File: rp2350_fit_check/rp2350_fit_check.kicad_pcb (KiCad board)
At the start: 6 copper layers, 118.8 x 73.4 mm, 364 parts, among them J1 Conn_01x05, J2 Conn_01x05, J3 Conn_01x05, J4 Conn_01x05, J5 Conn_01x04, SW1 SW_Push, SW2 SW_Push, U1 AP2112K-3.3, U2 RP2040, U3 W25Q16JVUXIQ_TR, Y1 12MHz

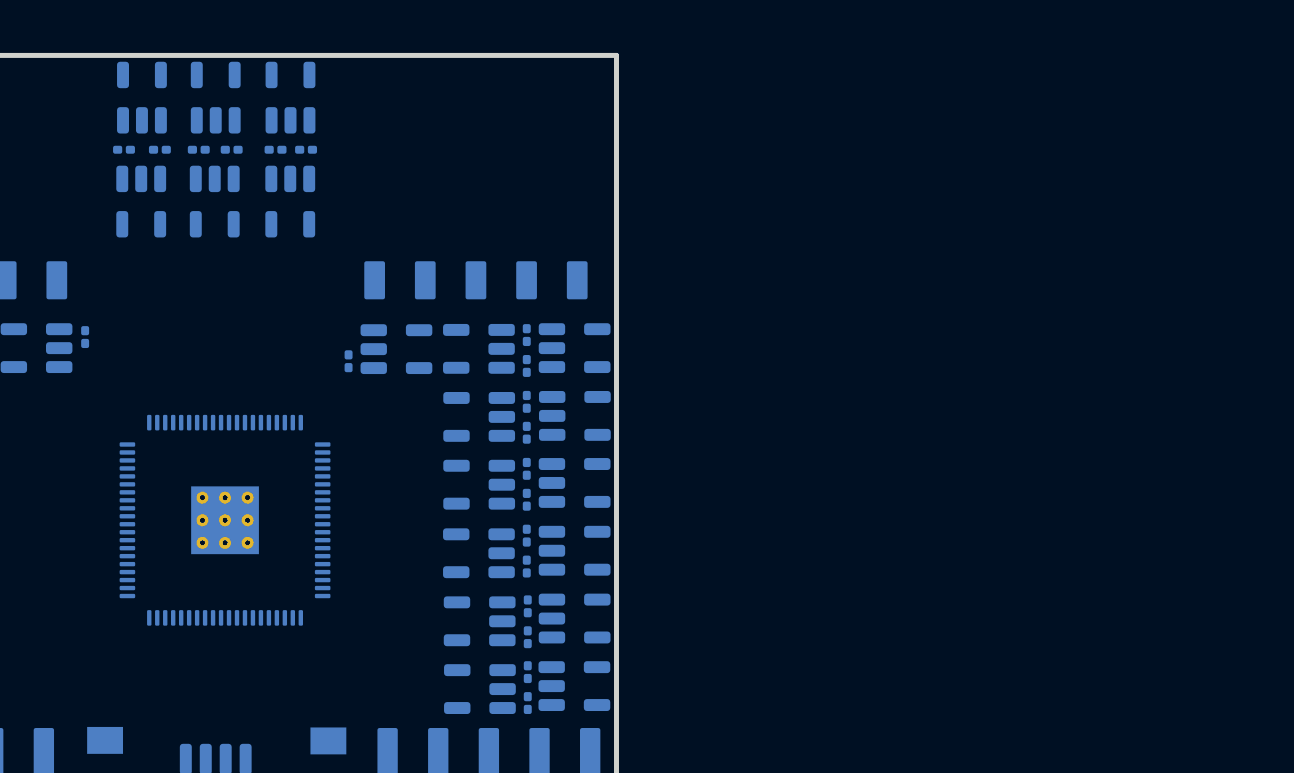
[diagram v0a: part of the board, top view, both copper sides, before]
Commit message: More work on rp2350 fit check.
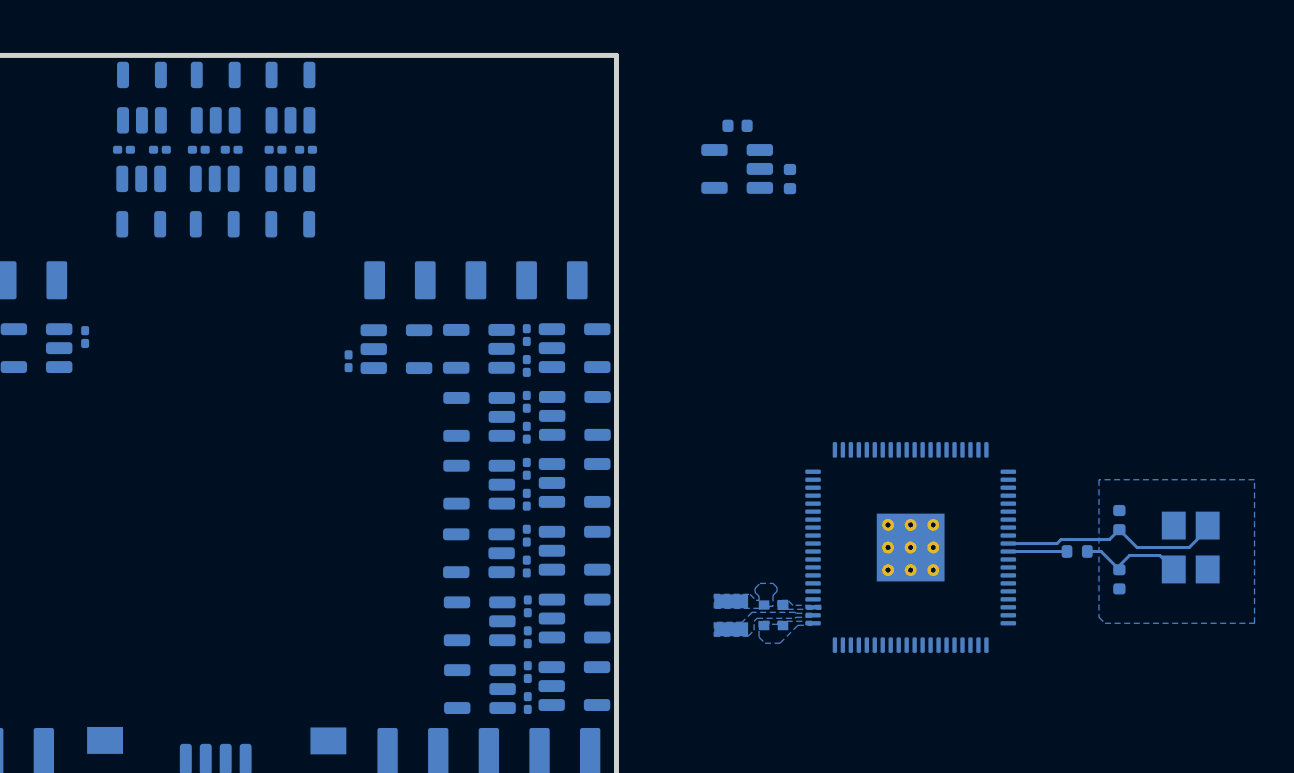
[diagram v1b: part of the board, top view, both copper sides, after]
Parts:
- added ?: , , B.Cu at (177.1, 110.6)
- added C1: 10uF, panel_custom:C_0402_1005Metric, B.Cu at (177.4, 89.3)
- added C2: 10uF, panel_custom:C_0402_1005Metric, B.Cu at (174.8, 86.6)
- added C3: 15p, Capacitor_SMD:C_0402_1005Metric, B.Cu at (194.0, 106.4)
- added C4: 15p, Capacitor_SMD:C_0402_1005Metric, B.Cu at (194.0, 109.3)
- added C6: 4.7u, RP2350_80QFN_minimal:C_0402_1005Metric_small_pads, B.Cu at (177.1, 111.2)
- added C7: 4.7u, RP2350_80QFN_minimal:C_0402_1005Metric_small_pads, B.Cu at (176.2, 111.2)
- added L1: 3.3u, RP2350_80QFN_minimal:L_pol_2016, B.Cu at (174.5, 111.2)
- added R2: 1k, Resistor_SMD:R_0402_1005Metric, B.Cu at (191.9, 108.0)
- added U1: AP2112K-3.3, Package_TO_SOT_SMD:SOT-23-5, B.Cu at (174.8, 88.8)
- added Y1: ABM8-272-T3, Crystal:Crystal_SMD_3225-4Pin_3.2x2.5mm, B.Cu at (197.6, 107.8)
- moved REF** 34.4 mm to (183.5, 107.8), turned to -90 degrees
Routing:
- net /XIN: track 0.00 -> 11.1 mm
- net Net-(C4-Pad1): track 0.00 -> 5.25 mm
- net /XOUT: track 0.00 -> 2.93 mm
- added copper zone on B.Cu, net +1V1
- added copper zone on B.Cu, net +3V3
- added copper zone on B.Cu, net /VREG_LX
- added copper zone on B.Cu, net GND

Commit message: Worked more on fit check / preliminary layout.
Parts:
- removed the C3 at (194.0, 106.4)
- removed the C4 at (194.0, 109.3)
- removed the R2 at (191.9, 108.0)
- added D1: LED, panel_custom:LED_0402_1005Metric, F.Cu at (130.0, 84.5)
- added D10: LED, panel_custom:LED_0402_1005Metric, F.Cu at (130.0, 107.0)
- added D100: LED, panel_custom:LED_0402_1005Metric, F.Cu at (145.0, 92.0)
- added D101: LED, panel_custom:LED_0402_1005Metric, F.Cu at (145.0, 94.5)
- added D102: LED, panel_custom:LED_0402_1005Metric, F.Cu at (145.0, 97.0)
- added D103: LED, panel_custom:LED_0402_1005Metric, F.Cu at (145.0, 99.5)
- added D104: LED, panel_custom:LED_0402_1005Metric, F.Cu at (145.0, 102.0)
- added D105: LED, panel_custom:LED_0402_1005Metric, F.Cu at (145.0, 104.5)
- added D106: LED, panel_custom:LED_0402_1005Metric, F.Cu at (145.0, 107.0)
- added D107: LED, panel_custom:LED_0402_1005Metric, F.Cu at (145.0, 109.5)
- added D108: LED, panel_custom:LED_0402_1005Metric, F.Cu at (145.0, 112.0)
- added D109: LED, panel_custom:LED_0402_1005Metric, F.Cu at (145.0, 114.5)
- added D11: LED, panel_custom:LED_0402_1005Metric, F.Cu at (130.0, 109.5)
- added D110: LED, panel_custom:LED_0402_1005Metric, F.Cu at (145.0, 117.0)
- added D111: LED, panel_custom:LED_0402_1005Metric, F.Cu at (145.0, 119.5)
- added D112: LED, panel_custom:LED_0402_1005Metric, F.Cu at (145.0, 122.0)
- added D113: LED, panel_custom:LED_0402_1005Metric, F.Cu at (147.5, 84.5)
- added D114: LED, panel_custom:LED_0402_1005Metric, F.Cu at (147.5, 87.0)
- added D115: LED, panel_custom:LED_0402_1005Metric, F.Cu at (147.5, 89.5)
- added D116: LED, panel_custom:LED_0402_1005Metric, F.Cu at (147.5, 92.0)
- added D117: LED, panel_custom:LED_0402_1005Metric, F.Cu at (147.5, 94.5)
- added D118: LED, panel_custom:LED_0402_1005Metric, F.Cu at (147.5, 97.0)
- added D119: LED, panel_custom:LED_0402_1005Metric, F.Cu at (147.5, 99.5)
- added D12: LED, panel_custom:LED_0402_1005Metric, F.Cu at (130.0, 112.0)
- added D120: LED, panel_custom:LED_0402_1005Metric, F.Cu at (147.5, 102.0)
- added D121: LED, panel_custom:LED_0402_1005Metric, F.Cu at (147.5, 104.5)
- added D122: LED, panel_custom:LED_0402_1005Metric, F.Cu at (147.5, 107.0)
- added D123: LED, panel_custom:LED_0402_1005Metric, F.Cu at (147.5, 109.5)
- added D124: LED, panel_custom:LED_0402_1005Metric, F.Cu at (147.5, 112.0)
- added D125: LED, panel_custom:LED_0402_1005Metric, F.Cu at (147.5, 114.5)
- added D126: LED, panel_custom:LED_0402_1005Metric, F.Cu at (147.5, 117.0)
- added D127: LED, panel_custom:LED_0402_1005Metric, F.Cu at (147.5, 119.5)
- added D128: LED, panel_custom:LED_0402_1005Metric, F.Cu at (147.5, 122.0)
- added D129: LED, panel_custom:LED_0402_1005Metric, F.Cu at (150.0, 84.5)
- added D13: LED, panel_custom:LED_0402_1005Metric, F.Cu at (130.0, 114.5)
- added D130: LED, panel_custom:LED_0402_1005Metric, F.Cu at (150.0, 87.0)
- added D131: LED, panel_custom:LED_0402_1005Metric, F.Cu at (150.0, 89.5)
- added D132: LED, panel_custom:LED_0402_1005Metric, F.Cu at (150.0, 92.0)
- added D133: LED, panel_custom:LED_0402_1005Metric, F.Cu at (150.0, 94.5)
- added D134: LED, panel_custom:LED_0402_1005Metric, F.Cu at (150.0, 97.0)
- added D135: LED, panel_custom:LED_0402_1005Metric, F.Cu at (150.0, 99.5)
- added D136: LED, panel_custom:LED_0402_1005Metric, F.Cu at (150.0, 102.0)
- added D137: LED, panel_custom:LED_0402_1005Metric, F.Cu at (150.0, 104.5)
- added D138: LED, panel_custom:LED_0402_1005Metric, F.Cu at (150.0, 107.0)
- added D139: LED, panel_custom:LED_0402_1005Metric, F.Cu at (150.0, 109.5)
- added D14: LED, panel_custom:LED_0402_1005Metric, F.Cu at (130.0, 117.0)
- added D140: LED, panel_custom:LED_0402_1005Metric, F.Cu at (150.0, 112.0)
- added D141: LED, panel_custom:LED_0402_1005Metric, F.Cu at (150.0, 114.5)
- added D142: LED, panel_custom:LED_0402_1005Metric, F.Cu at (150.0, 117.0)
- added D143: LED, panel_custom:LED_0402_1005Metric, F.Cu at (150.0, 119.5)
- added D144: LED, panel_custom:LED_0402_1005Metric, F.Cu at (150.0, 122.0)
- added D145: LED, panel_custom:LED_0402_1005Metric, F.Cu at (152.5, 84.5)
- added D146: LED, panel_custom:LED_0402_1005Metric, F.Cu at (152.5, 87.0)
- added D147: LED, panel_custom:LED_0402_1005Metric, F.Cu at (152.5, 89.5)
- added D148: LED, panel_custom:LED_0402_1005Metric, F.Cu at (152.5, 92.0)
- added D149: LED, panel_custom:LED_0402_1005Metric, F.Cu at (152.5, 94.5)
- added D15: LED, panel_custom:LED_0402_1005Metric, F.Cu at (130.0, 119.5)
- added D150: LED, panel_custom:LED_0402_1005Metric, F.Cu at (152.5, 97.0)
- added D151: LED, panel_custom:LED_0402_1005Metric, F.Cu at (152.5, 99.5)
- added D152: LED, panel_custom:LED_0402_1005Metric, F.Cu at (152.5, 102.0)
- added D153: LED, panel_custom:LED_0402_1005Metric, F.Cu at (152.5, 104.5)
- added D154: LED, panel_custom:LED_0402_1005Metric, F.Cu at (152.5, 107.0)
- added D155: LED, panel_custom:LED_0402_1005Metric, F.Cu at (152.5, 109.5)
- added D156: LED, panel_custom:LED_0402_1005Metric, F.Cu at (152.5, 112.0)
- added D157: LED, panel_custom:LED_0402_1005Metric, F.Cu at (152.5, 114.5)
- added D158: LED, panel_custom:LED_0402_1005Metric, F.Cu at (152.5, 117.0)
- added D159: LED, panel_custom:LED_0402_1005Metric, F.Cu at (152.5, 119.5)
- added D16: LED, panel_custom:LED_0402_1005Metric, F.Cu at (130.0, 122.0)
- added D160: LED, panel_custom:LED_0402_1005Metric, F.Cu at (152.5, 122.0)
- added D161: LED, panel_custom:LED_0402_1005Metric, F.Cu at (155.0, 84.5)
- added D162: LED, panel_custom:LED_0402_1005Metric, F.Cu at (155.0, 87.0)
- added D163: LED, panel_custom:LED_0402_1005Metric, F.Cu at (155.0, 89.5)
- added D164: LED, panel_custom:LED_0402_1005Metric, F.Cu at (155.0, 92.0)
- added D165: LED, panel_custom:LED_0402_1005Metric, F.Cu at (155.0, 94.5)
- added D166: LED, panel_custom:LED_0402_1005Metric, F.Cu at (155.0, 97.0)
- added D167: LED, panel_custom:LED_0402_1005Metric, F.Cu at (155.0, 99.5)
- added D168: LED, panel_custom:LED_0402_1005Metric, F.Cu at (155.0, 102.0)
- added D169: LED, panel_custom:LED_0402_1005Metric, F.Cu at (155.0, 104.5)
- added D17: LED, panel_custom:LED_0402_1005Metric, F.Cu at (132.5, 84.5)
- added D170: LED, panel_custom:LED_0402_1005Metric, F.Cu at (155.0, 107.0)
- added D171: LED, panel_custom:LED_0402_1005Metric, F.Cu at (155.0, 109.5)
- added D172: LED, panel_custom:LED_0402_1005Metric, F.Cu at (155.0, 112.0)
- added D173: LED, panel_custom:LED_0402_1005Metric, F.Cu at (155.0, 114.5)
- added D174: LED, panel_custom:LED_0402_1005Metric, F.Cu at (155.0, 117.0)
- added D175: LED, panel_custom:LED_0402_1005Metric, F.Cu at (155.0, 119.5)
- added D176: LED, panel_custom:LED_0402_1005Metric, F.Cu at (155.0, 122.0)
- added D177: LED, panel_custom:LED_0402_1005Metric, F.Cu at (157.5, 84.5)
- added D178: LED, panel_custom:LED_0402_1005Metric, F.Cu at (157.5, 87.0)
- added D179: LED, panel_custom:LED_0402_1005Metric, F.Cu at (157.5, 89.5)
- added D18: LED, panel_custom:LED_0402_1005Metric, F.Cu at (132.5, 87.0)
- added D180: LED, panel_custom:LED_0402_1005Metric, F.Cu at (157.5, 92.0)
- added D181: LED, panel_custom:LED_0402_1005Metric, F.Cu at (157.5, 94.5)
- added D182: LED, panel_custom:LED_0402_1005Metric, F.Cu at (157.5, 97.0)
- added D183: LED, panel_custom:LED_0402_1005Metric, F.Cu at (157.5, 99.5)
- added D184: LED, panel_custom:LED_0402_1005Metric, F.Cu at (157.5, 102.0)
- added D185: LED, panel_custom:LED_0402_1005Metric, F.Cu at (157.5, 104.5)
- added D186: LED, panel_custom:LED_0402_1005Metric, F.Cu at (157.5, 107.0)
- added D187: LED, panel_custom:LED_0402_1005Metric, F.Cu at (157.5, 109.5)
- added D188: LED, panel_custom:LED_0402_1005Metric, F.Cu at (157.5, 112.0)
- added D189: LED, panel_custom:LED_0402_1005Metric, F.Cu at (157.5, 114.5)
- added D19: LED, panel_custom:LED_0402_1005Metric, F.Cu at (132.5, 89.5)
- added D190: LED, panel_custom:LED_0402_1005Metric, F.Cu at (157.5, 117.0)
- added D191: LED, panel_custom:LED_0402_1005Metric, F.Cu at (157.5, 119.5)
- added D192: LED, panel_custom:LED_0402_1005Metric, F.Cu at (157.5, 122.0)
- added D193: LED, panel_custom:LED_0402_1005Metric, F.Cu at (160.0, 84.5)
- added D194: LED, panel_custom:LED_0402_1005Metric, F.Cu at (160.0, 87.0)
- added D195: LED, panel_custom:LED_0402_1005Metric, F.Cu at (160.0, 89.5)
- added D196: LED, panel_custom:LED_0402_1005Metric, F.Cu at (160.0, 92.0)
- added D197: LED, panel_custom:LED_0402_1005Metric, F.Cu at (160.0, 94.5)
- added D198: LED, panel_custom:LED_0402_1005Metric, F.Cu at (160.0, 97.0)
- added D199: LED, panel_custom:LED_0402_1005Metric, F.Cu at (160.0, 99.5)
- added D2: LED, panel_custom:LED_0402_1005Metric, F.Cu at (130.0, 87.0)
- added D20: LED, panel_custom:LED_0402_1005Metric, F.Cu at (132.5, 92.0)
- added D200: LED, panel_custom:LED_0402_1005Metric, F.Cu at (160.0, 102.0)
- added D201: LED, panel_custom:LED_0402_1005Metric, F.Cu at (160.0, 104.5)
- added D202: LED, panel_custom:LED_0402_1005Metric, F.Cu at (160.0, 107.0)
- added D203: LED, panel_custom:LED_0402_1005Metric, F.Cu at (160.0, 109.5)
- added D204: LED, panel_custom:LED_0402_1005Metric, F.Cu at (160.0, 112.0)
- added D205: LED, panel_custom:LED_0402_1005Metric, F.Cu at (160.0, 114.5)
- added D206: LED, panel_custom:LED_0402_1005Metric, F.Cu at (160.0, 117.0)
- added D207: LED, panel_custom:LED_0402_1005Metric, F.Cu at (160.0, 119.5)
- added D208: LED, panel_custom:LED_0402_1005Metric, F.Cu at (160.0, 122.0)
- added D209: LED, panel_custom:LED_0402_1005Metric, F.Cu at (162.5, 84.5)
- added D21: LED, panel_custom:LED_0402_1005Metric, F.Cu at (132.5, 94.5)
- added D210: LED, panel_custom:LED_0402_1005Metric, F.Cu at (162.5, 87.0)
- added D211: LED, panel_custom:LED_0402_1005Metric, F.Cu at (162.5, 89.5)
- added D212: LED, panel_custom:LED_0402_1005Metric, F.Cu at (162.5, 92.0)
- added D213: LED, panel_custom:LED_0402_1005Metric, F.Cu at (162.5, 94.5)
- added D214: LED, panel_custom:LED_0402_1005Metric, F.Cu at (162.5, 97.0)
- added D215: LED, panel_custom:LED_0402_1005Metric, F.Cu at (162.5, 99.5)
- added D216: LED, panel_custom:LED_0402_1005Metric, F.Cu at (162.5, 102.0)
- added D217: LED, panel_custom:LED_0402_1005Metric, F.Cu at (162.5, 104.5)
- added D218: LED, panel_custom:LED_0402_1005Metric, F.Cu at (162.5, 107.0)
- added D219: LED, panel_custom:LED_0402_1005Metric, F.Cu at (162.5, 109.5)
- added D22: LED, panel_custom:LED_0402_1005Metric, F.Cu at (132.5, 97.0)
- added D220: LED, panel_custom:LED_0402_1005Metric, F.Cu at (162.5, 112.0)
- added D221: LED, panel_custom:LED_0402_1005Metric, F.Cu at (162.5, 114.5)
- added D222: LED, panel_custom:LED_0402_1005Metric, F.Cu at (162.5, 117.0)
- added D223: LED, panel_custom:LED_0402_1005Metric, F.Cu at (162.5, 119.5)
- added D224: LED, panel_custom:LED_0402_1005Metric, F.Cu at (162.5, 122.0)
- added D225: LED, panel_custom:LED_0402_1005Metric, F.Cu at (165.0, 84.5)
- added D226: LED, panel_custom:LED_0402_1005Metric, F.Cu at (165.0, 87.0)
- added D227: LED, panel_custom:LED_0402_1005Metric, F.Cu at (165.0, 89.5)
- added D228: LED, panel_custom:LED_0402_1005Metric, F.Cu at (165.0, 92.0)
- added D229: LED, panel_custom:LED_0402_1005Metric, F.Cu at (165.0, 94.5)
- added D23: LED, panel_custom:LED_0402_1005Metric, F.Cu at (132.5, 99.5)
- added D230: LED, panel_custom:LED_0402_1005Metric, F.Cu at (165.0, 97.0)
- added D231: LED, panel_custom:LED_0402_1005Metric, F.Cu at (165.0, 99.5)
- added D232: LED, panel_custom:LED_0402_1005Metric, F.Cu at (165.0, 102.0)
- added D233: LED, panel_custom:LED_0402_1005Metric, F.Cu at (165.0, 104.5)
- added D234: LED, panel_custom:LED_0402_1005Metric, F.Cu at (165.0, 107.0)
- added D235: LED, panel_custom:LED_0402_1005Metric, F.Cu at (165.0, 109.5)
- added D236: LED, panel_custom:LED_0402_1005Metric, F.Cu at (165.0, 112.0)
- added D237: LED, panel_custom:LED_0402_1005Metric, F.Cu at (165.0, 114.5)
- added D238: LED, panel_custom:LED_0402_1005Metric, F.Cu at (165.0, 117.0)
- added D239: LED, panel_custom:LED_0402_1005Metric, F.Cu at (165.0, 119.5)
- added D24: LED, panel_custom:LED_0402_1005Metric, F.Cu at (132.5, 102.0)
- added D240: LED, panel_custom:LED_0402_1005Metric, F.Cu at (165.0, 122.0)
- added D241: LED, panel_custom:LED_0402_1005Metric, F.Cu at (167.5, 84.5)
- added D242: LED, panel_custom:LED_0402_1005Metric, F.Cu at (167.5, 87.0)
- added D243: LED, panel_custom:LED_0402_1005Metric, F.Cu at (167.5, 89.5)
- added D244: LED, panel_custom:LED_0402_1005Metric, F.Cu at (167.5, 92.0)
- added D245: LED, panel_custom:LED_0402_1005Metric, F.Cu at (167.5, 94.5)
- added D246: LED, panel_custom:LED_0402_1005Metric, F.Cu at (167.5, 97.0)
- added D247: LED, panel_custom:LED_0402_1005Metric, F.Cu at (167.5, 99.5)
- added D248: LED, panel_custom:LED_0402_1005Metric, F.Cu at (167.5, 102.0)
- added D249: LED, panel_custom:LED_0402_1005Metric, F.Cu at (167.5, 104.5)
- added D25: LED, panel_custom:LED_0402_1005Metric, F.Cu at (132.5, 104.5)
- added D250: LED, panel_custom:LED_0402_1005Metric, F.Cu at (167.5, 107.0)
- added D251: LED, panel_custom:LED_0402_1005Metric, F.Cu at (167.5, 109.5)
- added D252: LED, panel_custom:LED_0402_1005Metric, F.Cu at (167.5, 112.0)
- added D253: LED, panel_custom:LED_0402_1005Metric, F.Cu at (167.5, 114.5)
- added D254: LED, panel_custom:LED_0402_1005Metric, F.Cu at (167.5, 117.0)
- added D255: LED, panel_custom:LED_0402_1005Metric, F.Cu at (167.5, 119.5)
- added D256: LED, panel_custom:LED_0402_1005Metric, F.Cu at (167.5, 122.0)
- added D26: LED, panel_custom:LED_0402_1005Metric, F.Cu at (132.5, 107.0)
- added D27: LED, panel_custom:LED_0402_1005Metric, F.Cu at (132.5, 109.5)
- added D28: LED, panel_custom:LED_0402_1005Metric, F.Cu at (132.5, 112.0)
- added D29: LED, panel_custom:LED_0402_1005Metric, F.Cu at (132.5, 114.5)
- added D3: LED, panel_custom:LED_0402_1005Metric, F.Cu at (130.0, 89.5)
- added D30: LED, panel_custom:LED_0402_1005Metric, F.Cu at (132.5, 117.0)
- added D31: LED, panel_custom:LED_0402_1005Metric, F.Cu at (132.5, 119.5)
- added D32: LED, panel_custom:LED_0402_1005Metric, F.Cu at (132.5, 122.0)
- added D33: LED, panel_custom:LED_0402_1005Metric, F.Cu at (135.0, 84.5)
- added D34: LED, panel_custom:LED_0402_1005Metric, F.Cu at (135.0, 87.0)
- added D35: LED, panel_custom:LED_0402_1005Metric, F.Cu at (135.0, 89.5)
- added D36: LED, panel_custom:LED_0402_1005Metric, F.Cu at (135.0, 92.0)
- added D37: LED, panel_custom:LED_0402_1005Metric, F.Cu at (135.0, 94.5)
- added D38: LED, panel_custom:LED_0402_1005Metric, F.Cu at (135.0, 97.0)
- added D39: LED, panel_custom:LED_0402_1005Metric, F.Cu at (135.0, 99.5)
- added D4: LED, panel_custom:LED_0402_1005Metric, F.Cu at (130.0, 92.0)
- added D40: LED, panel_custom:LED_0402_1005Metric, F.Cu at (135.0, 102.0)
- added D41: LED, panel_custom:LED_0402_1005Metric, F.Cu at (135.0, 104.5)
- added D42: LED, panel_custom:LED_0402_1005Metric, F.Cu at (135.0, 107.0)
- added D43: LED, panel_custom:LED_0402_1005Metric, F.Cu at (135.0, 109.5)
- added D44: LED, panel_custom:LED_0402_1005Metric, F.Cu at (135.0, 112.0)
- added D45: LED, panel_custom:LED_0402_1005Metric, F.Cu at (135.0, 114.5)
- added D46: LED, panel_custom:LED_0402_1005Metric, F.Cu at (135.0, 117.0)
- added D47: LED, panel_custom:LED_0402_1005Metric, F.Cu at (135.0, 119.5)
- added D48: LED, panel_custom:LED_0402_1005Metric, F.Cu at (135.0, 122.0)
- added D49: LED, panel_custom:LED_0402_1005Metric, F.Cu at (137.5, 84.5)
- added D5: LED, panel_custom:LED_0402_1005Metric, F.Cu at (130.0, 94.5)
- added D50: LED, panel_custom:LED_0402_1005Metric, F.Cu at (137.5, 87.0)
- added D51: LED, panel_custom:LED_0402_1005Metric, F.Cu at (137.5, 89.5)
- added D52: LED, panel_custom:LED_0402_1005Metric, F.Cu at (137.5, 92.0)
- added D53: LED, panel_custom:LED_0402_1005Metric, F.Cu at (137.5, 94.5)
- added D54: LED, panel_custom:LED_0402_1005Metric, F.Cu at (137.5, 97.0)
- added D55: LED, panel_custom:LED_0402_1005Metric, F.Cu at (137.5, 99.5)
- added D56: LED, panel_custom:LED_0402_1005Metric, F.Cu at (137.5, 102.0)
- added D57: LED, panel_custom:LED_0402_1005Metric, F.Cu at (137.5, 104.5)
- added D58: LED, panel_custom:LED_0402_1005Metric, F.Cu at (137.5, 107.0)
- added D59: LED, panel_custom:LED_0402_1005Metric, F.Cu at (137.5, 109.5)
- added D6: LED, panel_custom:LED_0402_1005Metric, F.Cu at (130.0, 97.0)
- added D60: LED, panel_custom:LED_0402_1005Metric, F.Cu at (137.5, 112.0)
- added D61: LED, panel_custom:LED_0402_1005Metric, F.Cu at (137.5, 114.5)
- added D62: LED, panel_custom:LED_0402_1005Metric, F.Cu at (137.5, 117.0)
- added D63: LED, panel_custom:LED_0402_1005Metric, F.Cu at (137.5, 119.5)
- added D64: LED, panel_custom:LED_0402_1005Metric, F.Cu at (137.5, 122.0)
- added D65: LED, panel_custom:LED_0402_1005Metric, F.Cu at (140.0, 84.5)
- added D66: LED, panel_custom:LED_0402_1005Metric, F.Cu at (140.0, 87.0)
- added D67: LED, panel_custom:LED_0402_1005Metric, F.Cu at (140.0, 89.5)
- added D68: LED, panel_custom:LED_0402_1005Metric, F.Cu at (140.0, 92.0)
- added D69: LED, panel_custom:LED_0402_1005Metric, F.Cu at (140.0, 94.5)
- added D7: LED, panel_custom:LED_0402_1005Metric, F.Cu at (130.0, 99.5)
- added D70: LED, panel_custom:LED_0402_1005Metric, F.Cu at (140.0, 97.0)
- added D71: LED, panel_custom:LED_0402_1005Metric, F.Cu at (140.0, 99.5)
- added D72: LED, panel_custom:LED_0402_1005Metric, F.Cu at (140.0, 102.0)
- added D73: LED, panel_custom:LED_0402_1005Metric, F.Cu at (140.0, 104.5)
- added D74: LED, panel_custom:LED_0402_1005Metric, F.Cu at (140.0, 107.0)
- added D75: LED, panel_custom:LED_0402_1005Metric, F.Cu at (140.0, 109.5)
- added D76: LED, panel_custom:LED_0402_1005Metric, F.Cu at (140.0, 112.0)
- added D77: LED, panel_custom:LED_0402_1005Metric, F.Cu at (140.0, 114.5)
- added D78: LED, panel_custom:LED_0402_1005Metric, F.Cu at (140.0, 117.0)
- added D79: LED, panel_custom:LED_0402_1005Metric, F.Cu at (140.0, 119.5)
- added D8: LED, panel_custom:LED_0402_1005Metric, F.Cu at (130.0, 102.0)
- added D80: LED, panel_custom:LED_0402_1005Metric, F.Cu at (140.0, 122.0)
- added D81: LED, panel_custom:LED_0402_1005Metric, F.Cu at (142.5, 84.5)
- added D82: LED, panel_custom:LED_0402_1005Metric, F.Cu at (142.5, 87.0)
- added D83: LED, panel_custom:LED_0402_1005Metric, F.Cu at (142.5, 89.5)
- added D84: LED, panel_custom:LED_0402_1005Metric, F.Cu at (142.5, 92.0)
- added D85: LED, panel_custom:LED_0402_1005Metric, F.Cu at (142.5, 94.5)
- added D86: LED, panel_custom:LED_0402_1005Metric, F.Cu at (142.5, 97.0)
- added D87: LED, panel_custom:LED_0402_1005Metric, F.Cu at (142.5, 99.5)
- added D88: LED, panel_custom:LED_0402_1005Metric, F.Cu at (142.5, 102.0)
- added D89: LED, panel_custom:LED_0402_1005Metric, F.Cu at (142.5, 104.5)
- added D9: LED, panel_custom:LED_0402_1005Metric, F.Cu at (130.0, 104.5)
- added D90: LED, panel_custom:LED_0402_1005Metric, F.Cu at (142.5, 107.0)
- added D91: LED, panel_custom:LED_0402_1005Metric, F.Cu at (142.5, 109.5)
- added D92: LED, panel_custom:LED_0402_1005Metric, F.Cu at (142.5, 112.0)
- added D93: LED, panel_custom:LED_0402_1005Metric, F.Cu at (142.5, 114.5)
- added D94: LED, panel_custom:LED_0402_1005Metric, F.Cu at (142.5, 117.0)
- added D95: LED, panel_custom:LED_0402_1005Metric, F.Cu at (142.5, 119.5)
- added D96: LED, panel_custom:LED_0402_1005Metric, F.Cu at (142.5, 122.0)
- added D97: LED, panel_custom:LED_0402_1005Metric, F.Cu at (145.0, 84.5)
- added D98: LED, panel_custom:LED_0402_1005Metric, F.Cu at (145.0, 87.0)
- added D99: LED, panel_custom:LED_0402_1005Metric, F.Cu at (145.0, 89.5)
- added REF**: R_0201_0603Metric, Resistor_SMD:R_0201_0603Metric, F.Cu at (160.0, 85.8)
- added REF**: R_0201_0603Metric, Resistor_SMD:R_0201_0603Metric, F.Cu at (142.4, 85.8)
- added REF**: R_0201_0603Metric, Resistor_SMD:R_0201_0603Metric, F.Cu at (132.4, 85.8)
- added REF**: R_0201_0603Metric, Resistor_SMD:R_0201_0603Metric, F.Cu at (129.9, 85.8)
- added REF**: R_0201_0603Metric, Resistor_SMD:R_0201_0603Metric, F.Cu at (154.9, 85.8)
- added REF**: R_0201_0603Metric, Resistor_SMD:R_0201_0603Metric, F.Cu at (157.5, 85.8)
- added REF**: R_0201_0603Metric, Resistor_SMD:R_0201_0603Metric, F.Cu at (147.5, 85.8)
- added REF**: R_0201_0603Metric, Resistor_SMD:R_0201_0603Metric, F.Cu at (139.9, 85.8)
- added REF**: R_0201_0603Metric, Resistor_SMD:R_0201_0603Metric, F.Cu at (135.0, 85.8)
- added REF**: R_0201_0603Metric, Resistor_SMD:R_0201_0603Metric, F.Cu at (167.5, 85.8)
- added REF**: C_0201_0603Metric, Capacitor_SMD:C_0201_0603Metric, B.Cu at (153.9, 113.1)
- added REF**: R_0201_0603Metric, Resistor_SMD:R_0201_0603Metric, F.Cu at (52.5, 52.5)
- added REF**: C_0201_0603Metric, Capacitor_SMD:C_0201_0603Metric, B.Cu at (142.3, 104.4)
- added REF**: R_0201_0603Metric, Resistor_SMD:R_0201_0603Metric, B.Cu at (143.1, 116.8)
- added REF**: C_0201_0603Metric, Capacitor_SMD:C_0201_0603Metric, B.Cu at (155.1, 102.4)
- added REF**: R_0201_0603Metric, Resistor_SMD:R_0201_0603Metric, F.Cu at (149.9, 85.8)
- added REF**: C_0201_0603Metric, Capacitor_SMD:C_0201_0603Metric, B.Cu at (142.4, 106.3)
- added REF**: C_0201_0603Metric, Capacitor_SMD:C_0201_0603Metric, B.Cu at (147.3, 98.1)
- added REF**: R_0201_0603Metric, Resistor_SMD:R_0201_0603Metric, F.Cu at (137.4, 85.8)
- added REF**: R_0201_0603Metric, Resistor_SMD:R_0201_0603Metric, B.Cu at (154.2, 116.8)
- added REF**: R_0201_0603Metric, Resistor_SMD:R_0201_0603Metric, B.Cu at (148.9, 99.7)
- added REF**: C_0201_0603Metric, Capacitor_SMD:C_0201_0603Metric, B.Cu at (139.3, 115.6)
- added REF**: R_0201_0603Metric, Resistor_SMD:R_0201_0603Metric, F.Cu at (165.0, 85.8)
- added REF**: C_0201_0603Metric, Capacitor_SMD:C_0201_0603Metric, B.Cu at (155.2, 105.9)
- added REF**: C_0201_0603Metric, Capacitor_SMD:C_0201_0603Metric, B.Cu at (146.1, 99.8)
- added REF**: C_0201_0603Metric, Capacitor_SMD:C_0201_0603Metric, B.Cu at (149.5, 112.5)
- added REF**: R_0201_0603Metric, Resistor_SMD:R_0201_0603Metric, F.Cu at (152.5, 85.8)
- added REF**: R_0201_0603Metric, Resistor_SMD:R_0201_0603Metric, B.Cu at (153.9, 114.6)
- added REF**: C_0201_0603Metric, Capacitor_SMD:C_0201_0603Metric, B.Cu at (149.7, 99.8)
- added REF**: C_0201_0603Metric, Capacitor_SMD:C_0201_0603Metric, B.Cu at (142.4, 108.4)
- added REF**: R_0201_0603Metric, Resistor_SMD:R_0201_0603Metric, B.Cu at (139.5, 111.2)
- added REF**: flashmem_PSON50P300X200X60-9N, panel_custom:flashmem_PSON50P300X200X60-9N, B.Cu at (140.7, 113.4)
- added REF**: C_0201_0603Metric, Capacitor_SMD:C_0201_0603Metric, B.Cu at (148.1, 99.7)
- added REF**: R_0201_0603Metric, Resistor_SMD:R_0201_0603Metric, F.Cu at (145.0, 85.8)
- added REF**: C_0201_0603Metric, Capacitor_SMD:C_0201_0603Metric, B.Cu at (150.1, 98.1)
- added REF**: C_0201_0603Metric, Capacitor_SMD:C_0201_0603Metric, B.Cu at (155.1, 109.6)
- added REF**: C_0201_0603Metric, Capacitor_SMD:C_0201_0603Metric, B.Cu at (146.5, 112.5)
- added REF**: R_0201_0603Metric, Resistor_SMD:R_0201_0603Metric, F.Cu at (162.5, 85.8)
- added REF**: C_0201_0603Metric, Capacitor_SMD:C_0201_0603Metric, B.Cu at (155.2, 106.7)
- moved Y1 50.4 mm to (148.7, 95.4), turned to 0 degrees
- moved REF** 34.8 mm to (148.7, 106.1), turned to 0 degrees
- moved C1 33.2 mm to (157.3, 115.7), turned to 0 degrees
- moved U1 29.8 mm to (157.8, 113.2), turned to 90 degrees
- moved C2 29.2 mm to (158.3, 110.7), turned to 180 degrees
- moved ? 25.6 mm to (151.6, 112.5), turned to 0 degrees
- moved C6 25.0 mm to (152.1, 112.5), turned to 0 degrees
- moved C7 24.2 mm to (152.1, 113.5), turned to 0 degrees
- moved L1 22.8 mm to (152.1, 115.2), turned to 0 degrees
- moved SW2 11.3 mm to (143.1, 120.1)
- moved SW1 11.1 mm to (154.2, 120.1), turned to -90 degrees
- moved REF** 6.86 mm to (164.2, 100.3)
- moved REF** 6.85 mm to (161.8, 101.2)
- moved REF** 6.81 mm to (164.2, 107.3)
- moved REF** 6.81 mm to (161.9, 108.0)
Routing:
- net /XIN: track 11.1 -> 0.00 mm
- net Net-(C4-Pad1): track 5.25 -> 0.00 mm
- net /XOUT: track 2.93 -> 0.00 mm

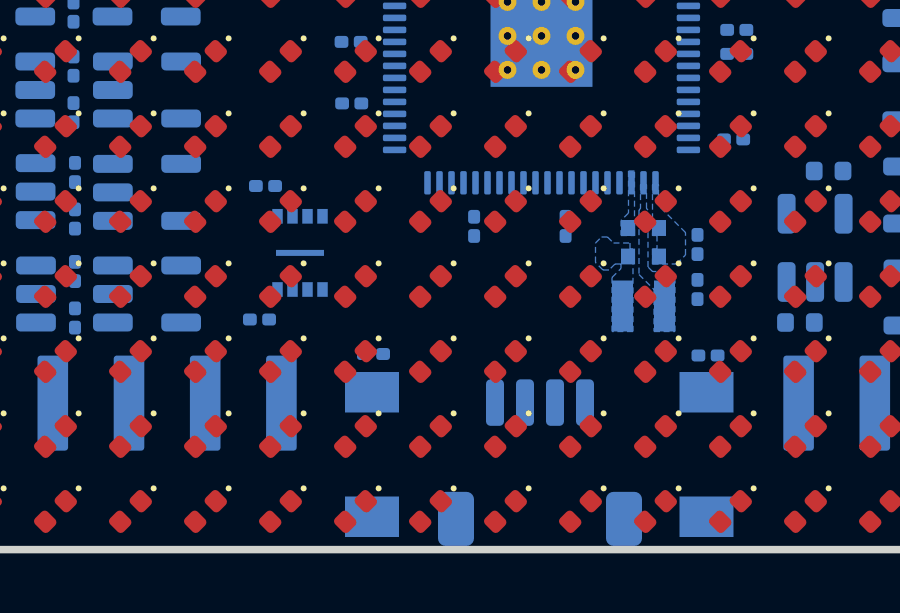
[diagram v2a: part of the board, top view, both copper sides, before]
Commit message: Finished fit check layout for rp2350 design.
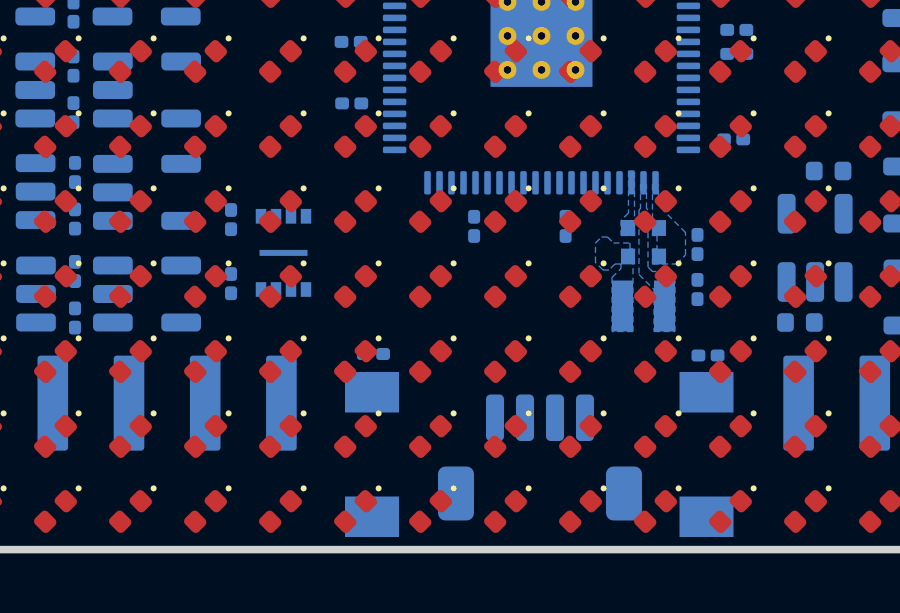
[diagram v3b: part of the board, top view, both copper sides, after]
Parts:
- removed the J5 at (148.7, 120.4)
- added REF**: JST_SH_BM04B-SRSS-TB_1x04-1MP_P1.00mm_Vertical, panel_custom:JST_SH_BM04B-SRSS-TB_1x04-1MP_P1.00mm_Vertical, B.Cu at (148.7, 120.2)
- L1: value 3.3u -> 4.7u
- moved REF** 1.61 mm to (138.3, 112.3), turned to -90 degrees
- moved REF** 1.53 mm to (138.3, 114.4), turned to 90 degrees
- moved REF** 0.55 mm to (140.1, 113.4)
- turned L1 to 180 degrees
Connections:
- L1 pad 1: +1V1 -> (no net)
- L1 pad 2: /VREG_LX -> (no net)
